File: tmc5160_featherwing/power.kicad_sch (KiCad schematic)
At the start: 0 parts

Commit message: Add connectors
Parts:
- added J1: Conn_TERM_HDR_01x02_Pin_5.0MM_Horizontal, Janelia:PhoenixContact_MSTBA_2,5_2-G_1x02_P5.00mm_Horizontal, symbol Janelia:Conn_TERM_HDR_01x02_Pin_5.0MM_Horizontal
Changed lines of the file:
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@@
   (title_block
     (title "tmc5160_featherwing")
-    (date "2024-03-22")
+    (date "2024-03-25")
     (rev "1.0")
     (company "Howard Hughes Medical Institute")
   )
+  (symbol (lib_id "Janelia:Conn_TERM_HDR_01x02_Pin_5.0MM_Horizontal") (at 73.66 88.9 0) (unit 1)
+    (in_bom yes) (on_board yes) (dnp no) (fields_autoplaced)
+    (property "Reference" "J1" (at 74.295 86.36 0)
+      (effects (font (size 1.27 1.27)))
+    )
+    (property "Value" "Conn_TERM_HDR_01x02_Pin_5.0MM_Horizontal" (at 73.66 101.6 0)
+      (effects (font (size 1.27 1.27)) hide)
+    )
+    (property "Footprint" "Janelia:PhoenixContact_MSTBA_2,5_2-G_1x02_P5.00mm_Horizontal" (at 73.66 53.34 0)
+      (effects (font (size 1.27 1.27)) hide)
+    )
+    (property "Datasheet" "" (at 73.66 67.31 0)
+      (effects (font (size 1.27 1.27)) hide)
+    )
+    (property "Manufacturer" "Phoenix Contact" (at 73.66 55.88 0)
+      (effects (font (size 1.27 1.27)) hide)
+    )
+    (property "Manufacturer Part Number" "1757475" (at 73.66 60.96 0)
+      (effects (font (size 1.27 1.27)) hide)
+    )
+    (property "Description" "TERM BLOCK HDR 2POS 90DEG 5MM" (at 73.66 63.5 0)
+      (effects (font (size 1.27 1.27)) hide)
+    )
+    (property "Vendor" "Digi-Key" (at 73.66 58.42 0)
+      (effects (font (size 1.27 1.27)) hide)
+    )
+    (property "Vendor Part Number" "277-1117-ND" (at 73.66 66.04 0)
+      (effects (font (size 1.27 1.27)) hide)
+    )
+    (property "Sim.Enable" "0" (at 73.66 88.9 0)
+      (effects (font (size 1.27 1.27)) hide)
+    )
+    (pin "1")
+    (pin "2")
+    (instances
+      (project "tmc5160_featherwing"
+        (path "/df2b2e89-e055-4140-95de-f1df723db034/c1dd8f61-494c-402f-8e59-08309c64fc3f"
+          (reference "J1") (unit 1)
+        )
+      )
+    )
+  )
 )

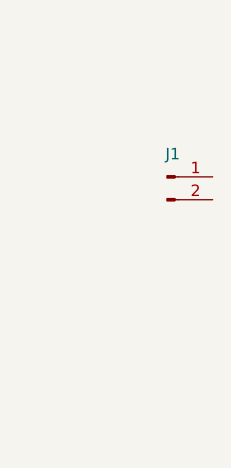
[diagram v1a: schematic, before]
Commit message: Change connectors
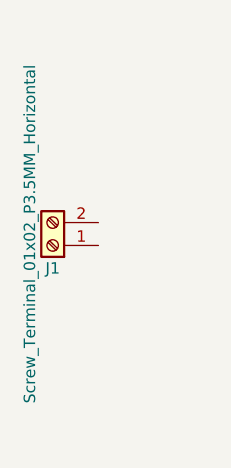
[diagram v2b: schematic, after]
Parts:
- removed J1: Conn_TERM_HDR_01x02_Pin_5.0MM_Horizontal, Janelia:PhoenixContact_MSTBA_2,5_2-G_1x02_P5.00mm_Horizontal, symbol Janelia:Conn_TERM_HDR_01x02_Pin_5.0MM_Horizontal
- added J1: Screw_Terminal_01x02_P3.5MM_Horizontal, Janelia:TerminalBlock_Phoenix_PT-1,5-2-3.5-H_1x02_P3.50mm_Horizontal, symbol Janelia:Screw_Terminal_01x02_P3.5MM_Horizontal
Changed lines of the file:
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@@
     (company "Howard Hughes Medical Institute")
   )
-  (symbol (lib_id "Janelia:Conn_TERM_HDR_01x02_Pin_5.0MM_Horizontal") (at 73.66 88.9 0) (unit 1)
+  (symbol (lib_id "Janelia:Screw_Terminal_01x02_P3.5MM_Horizontal") (at 60.96 96.52 180) (unit 1)
     (in_bom yes) (on_board yes) (dnp no) (fields_autoplaced)
-    (property "Reference" "J1" (at 74.295 86.36 0)
+    (property "Reference" "J1" (at 60.96 99.06 0) (do_not_autoplace)
       (effects (font (size 1.27 1.27)))
     )
-    (property "Value" "Conn_TERM_HDR_01x02_Pin_5.0MM_Horizontal" (at 73.66 101.6 0)
+    (property "Value" "Screw_Terminal_01x02_P3.5MM_Horizontal" (at 58.42 95.25 90) (do_not_autoplace)
+      (effects (font (size 1.27 1.27)))
+    )
+    (property "Footprint" "Janelia:TerminalBlock_Phoenix_PT-1,5-2-3.5-H_1x02_P3.50mm_Horizontal" (at 60.96 96.52 0)
       (effects (font (size 1.27 1.27)) hide)
     )
-    (property "Footprint" "Janelia:PhoenixContact_MSTBA_2,5_2-G_1x02_P5.00mm_Horizontal" (at 73.66 53.34 0)
+    (property "Datasheet" "~" (at 60.96 96.52 0)
       (effects (font (size 1.27 1.27)) hide)
     )
-    (property "Datasheet" "" (at 73.66 67.31 0)
+    (property "Description" "TERM BLK 2POS SIDE ENT 3.5MM PCB" (at 60.96 96.52 0)
       (effects (font (size 1.27 1.27)) hide)
     )
-    (property "Manufacturer" "Phoenix Contact" (at 73.66 55.88 0)
+    (property "Manufacturer" "Phoenix Contact" (at 60.96 96.52 0)
       (effects (font (size 1.27 1.27)) hide)
     )
-    (property "Manufacturer Part Number" "1757475" (at 73.66 60.96 0)
+    (property "Manufacturer Part Number" "1984617" (at 60.96 96.52 0)
       (effects (font (size 1.27 1.27)) hide)
     )
-    (property "Description" "TERM BLOCK HDR 2POS 90DEG 5MM" (at 73.66 63.5 0)
+    (property "Vendor" "Digi-Key" (at 60.96 96.52 0)
       (effects (font (size 1.27 1.27)) hide)
     )
-    (property "Vendor" "Digi-Key" (at 73.66 58.42 0)
+    (property "Vendor Part Number" "277-1721-ND" (at 60.96 96.52 0)
       (effects (font (size 1.27 1.27)) hide)
     )
-    (property "Vendor Part Number" "277-1117-ND" (at 73.66 66.04 0)
-      (effects (font (size 1.27 1.27)) hide)
-    )
-    (property "Sim.Enable" "0" (at 73.66 88.9 0)
-      (effects (font (size 1.27 1.27)) hide)
-    )

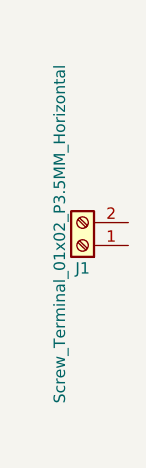
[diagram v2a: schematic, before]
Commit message: Switch back to terminal blocks
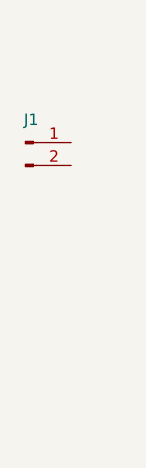
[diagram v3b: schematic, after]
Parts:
- removed J1: Screw_Terminal_01x02_P3.5MM_Horizontal, Janelia:TerminalBlock_Phoenix_PT-1,5-2-3.5-H_1x02_P3.50mm_Horizontal, symbol Janelia:Screw_Terminal_01x02_P3.5MM_Horizontal
- added J1: Conn_TERM_HDR_01x02_Pin_3.5MM_Horizontal, Janelia:PhoenixContact_MC_1,5_2-G-3.5_1x02_P3.50mm_Horizontal, symbol Janelia:Conn_TERM_HDR_01x02_Pin_3.5MM_Horizontal
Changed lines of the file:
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@@
     (company "Howard Hughes Medical Institute")
   )
-  (symbol (lib_id "Janelia:Screw_Terminal_01x02_P3.5MM_Horizontal") (at 60.96 96.52 180) (unit 1)
+  (symbol (lib_id "Janelia:Conn_TERM_HDR_01x02_Pin_3.5MM_Horizontal") (at 54.61 85.09 0) (unit 1)
     (in_bom yes) (on_board yes) (dnp no) (fields_autoplaced)
-    (property "Reference" "J1" (at 60.96 99.06 0) (do_not_autoplace)
+    (property "Reference" "J1" (at 55.245 82.55 0)
       (effects (font (size 1.27 1.27)))
     )
-    (property "Value" "Screw_Terminal_01x02_P3.5MM_Horizontal" (at 58.42 95.25 90) (do_not_autoplace)
-      (effects (font (size 1.27 1.27)))
-    )
-    (property "Footprint" "Janelia:TerminalBlock_Phoenix_PT-1,5-2-3.5-H_1x02_P3.50mm_Horizontal" (at 60.96 96.52 0)
+    (property "Value" "Conn_TERM_HDR_01x02_Pin_3.5MM_Horizontal" (at 54.61 97.79 0)
       (effects (font (size 1.27 1.27)) hide)
     )
-    (property "Datasheet" "~" (at 60.96 96.52 0)
+    (property "Footprint" "Janelia:PhoenixContact_MC_1,5_2-G-3.5_1x02_P3.50mm_Horizontal" (at 54.61 49.53 0)
       (effects (font (size 1.27 1.27)) hide)
     )
-    (property "Description" "TERM BLK 2POS SIDE ENT 3.5MM PCB" (at 60.96 96.52 0)
+    (property "Datasheet" "" (at 54.61 63.5 0)
       (effects (font (size 1.27 1.27)) hide)
     )
-    (property "Manufacturer" "Phoenix Contact" (at 60.96 96.52 0)
+    (property "Manufacturer" "Phoenix Contact" (at 54.61 52.07 0)
       (effects (font (size 1.27 1.27)) hide)
     )
-    (property "Manufacturer Part Number" "1984617" (at 60.96 96.52 0)
+    (property "Manufacturer Part Number" "1844210" (at 54.61 57.15 0)
       (effects (font (size 1.27 1.27)) hide)
     )
-    (property "Vendor" "Digi-Key" (at 60.96 96.52 0)
+    (property "Description" "TERM BLOCK HDR 2POS 90DEG 3.5MM" (at 54.61 59.69 0)
       (effects (font (size 1.27 1.27)) hide)
     )
-    (property "Vendor Part Number" "277-1721-ND" (at 60.96 96.52 0)
+    (property "Vendor" "Digi-Key" (at 54.61 54.61 0)
       (effects (font (size 1.27 1.27)) hide)
     )
+    (property "Vendor Part Number" "277-2416-ND" (at 54.61 62.23 0)
+      (effects (font (size 1.27 1.27)) hide)
+    )
+    (property "Sim.Enable" "0" (at 54.61 85.09 0)
+      (effects (font (size 1.27 1.27)) hide)
+    )
+    (pin "2")
     (pin "1")
-    (pin "2")
     (instances
       (project "tmc5160_featherwing"

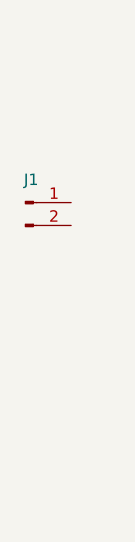
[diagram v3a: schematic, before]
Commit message: Adjust connectors
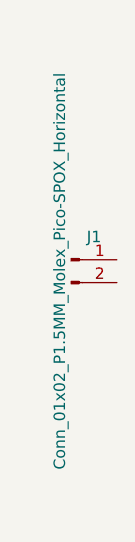
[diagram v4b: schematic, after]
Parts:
- removed J1: Conn_TERM_HDR_01x02_Pin_3.5MM_Horizontal, Janelia:PhoenixContact_MC_1,5_2-G-3.5_1x02_P3.50mm_Horizontal, symbol Janelia:Conn_TERM_HDR_01x02_Pin_3.5MM_Horizontal
- added J1: Conn_01x02_P1.5MM_Molex_Pico-SPOX_Horizontal, Janelia:Molex_Pico-SPOX_87438_1x02-P1.5MM_Horizontal, symbol Janelia:Conn_01x02_P1.5MM_Molex_Pico-SPOX_Horizontal
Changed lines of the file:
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@@
   (title_block
     (title "tmc5160_featherwing")
-    (date "2024-03-25")
+    (date "2024-04-04")
     (rev "1.0")
     (company "Howard Hughes Medical Institute")
   )
-  (symbol (lib_id "Janelia:Conn_TERM_HDR_01x02_Pin_3.5MM_Horizontal") (at 54.61 85.09 0) (unit 1)
+  (symbol (lib_id "Janelia:Conn_01x02_P1.5MM_Molex_Pico-SPOX_Horizontal") (at 59.69 91.44 0) (unit 1)
     (in_bom yes) (on_board yes) (dnp no) (fields_autoplaced)
-    (property "Reference" "J1" (at 55.245 82.55 0)
+    (property "Reference" "J1" (at 62.23 88.9 0) (do_not_autoplace)
       (effects (font (size 1.27 1.27)))
     )
-    (property "Value" "Conn_TERM_HDR_01x02_Pin_3.5MM_Horizontal" (at 54.61 97.79 0)
+    (property "Value" "Conn_01x02_P1.5MM_Molex_Pico-SPOX_Horizontal" (at 58.42 92.71 90) (do_not_autoplace)
+      (effects (font (size 1.27 1.27)))
+    )
+    (property "Footprint" "Janelia:Molex_Pico-SPOX_87438_1x02-P1.5MM_Horizontal" (at 59.69 91.44 0)
       (effects (font (size 1.27 1.27)) hide)
     )
-    (property "Footprint" "Janelia:PhoenixContact_MC_1,5_2-G-3.5_1x02_P3.50mm_Horizontal" (at 54.61 49.53 0)
+    (property "Datasheet" "~" (at 59.69 91.44 0)
       (effects (font (size 1.27 1.27)) hide)
     )
-    (property "Datasheet" "" (at 54.61 63.5 0)
+    (property "Description" "CONN HEADER SMD R/A 2POS 1.5MM" (at 59.69 91.44 0)
       (effects (font (size 1.27 1.27)) hide)
     )
-    (property "Manufacturer" "Phoenix Contact" (at 54.61 52.07 0)
+    (property "Manufacturer" "Molex" (at 59.69 91.44 0)
       (effects (font (size 1.27 1.27)) hide)
     )
-    (property "Manufacturer Part Number" "1844210" (at 54.61 57.15 0)
+    (property "Manufactuer Part Number" "0874380243" (at 59.69 91.44 0)
       (effects (font (size 1.27 1.27)) hide)
     )
-    (property "Description" "TERM BLOCK HDR 2POS 90DEG 3.5MM" (at 54.61 59.69 0)
+    (property "Vendor" "Digi-Key" (at 59.69 91.44 0)
       (effects (font (size 1.27 1.27)) hide)
     )
-    (property "Vendor" "Digi-Key" (at 54.61 54.61 0)
+    (property "Vendor Part Number" "WM7646CT-ND" (at 59.69 91.44 0)
       (effects (font (size 1.27 1.27)) hide)
     )
-    (property "Vendor Part Number" "277-2416-ND" (at 54.61 62.23 0)
-      (effects (font (size 1.27 1.27)) hide)
-    )
-    (property "Sim.Enable" "0" (at 54.61 85.09 0)
-      (effects (font (size 1.27 1.27)) hide)
-    )
+    (pin "1")
     (pin "2")
-    (pin "1")
     (instances
       (project "tmc5160_featherwing"

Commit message: Add to power sheet
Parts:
- removed J1: Conn_01x02_P1.5MM_Molex_Pico-SPOX_Horizontal, Janelia:Molex_Pico-SPOX_87438_1x02-P1.5MM_Horizontal, symbol Janelia:Conn_01x02_P1.5MM_Molex_Pico-SPOX_Horizontal
- added C1: 100uF_63V, Janelia:CP_Elec_10x10.5, symbol Janelia:CP_100uF_63V_10x10.5MM
- added C2: 10uF_100V, Janelia:C_1210_3225Metric, symbol Janelia:C_10uF_100V_1210
- added C3: 10uF_6.3V, Janelia:C_0402_1005Metric, symbol Janelia:C_10uF_6.3V_0402
- added J1, J3: Conn_01x03_P2.54MM_HeaderHoles, Janelia:PinHeader_1x03_P2.54mm_Vertical_Holes, symbol Janelia:Conn_01x03_P2.54MM_HeaderHoles
- added J2: Conn_01x02_P1.5MM_Molex_Pico-SPOX-87438_Horizontal, Janelia:Molex_Pico-SPOX-87438_1x02-P1.5MM_Horizontal, symbol Janelia:Conn_01x02_P1.5MM_Molex_Pico-SPOX-87438_Horizontal
- added U10: 3.3V_100MA, Janelia:DRB0008B, symbol Janelia:Regulator_Linear_3.3V_100MA_60Vin
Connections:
- new net ENABLE: U10.5 (EN)
- new net GND: C1.2, C2.2, C3.2, J2.2 (Pin_2), J3.1 (Pin_1), J3.2 (Pin_2), J3.3 (Pin_3), U10.4 (GND), U10.9 (PAD)
- new net VIO: C3.1, U10.1 (OUT)
- new net VM: C1.1, C2.1, J1.1 (Pin_1), J1.2 (Pin_2), J1.3 (Pin_3), J2.1 (Pin_1), U10.8 (IN)
- no-connect marks 0 -> 2

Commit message: Add parts
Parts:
- added C2: 100uF_63V, Janelia:CP_Elec_10x10.5, symbol Janelia:CP_100uF_63V_10x10.5MM
- added D1: Diode_SMAJ51A, Janelia:D_SMA, symbol Janelia:Diode_SMAJ51A
- renumbered C2 to C3, C3 to C4
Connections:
- net GND: now also J1.1 (Pin_1), J1.2 (Pin_2), J1.3 (Pin_3), J2.1 (Pin_1), C2.2, D1.2 (A2); no longer J2.2 (Pin_2), J3.1 (Pin_1), J3.2 (Pin_2), J3.3 (Pin_3)
- net VM: now also J2.2 (Pin_2), J3.1 (Pin_1), J3.2 (Pin_2), J3.3 (Pin_3), C2.1, D1.1 (A1); no longer J1.1 (Pin_1), J1.2 (Pin_2), J1.3 (Pin_3), J2.1 (Pin_1)
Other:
- moved on the sheet: C3, C4, J1, J2, J3, U10

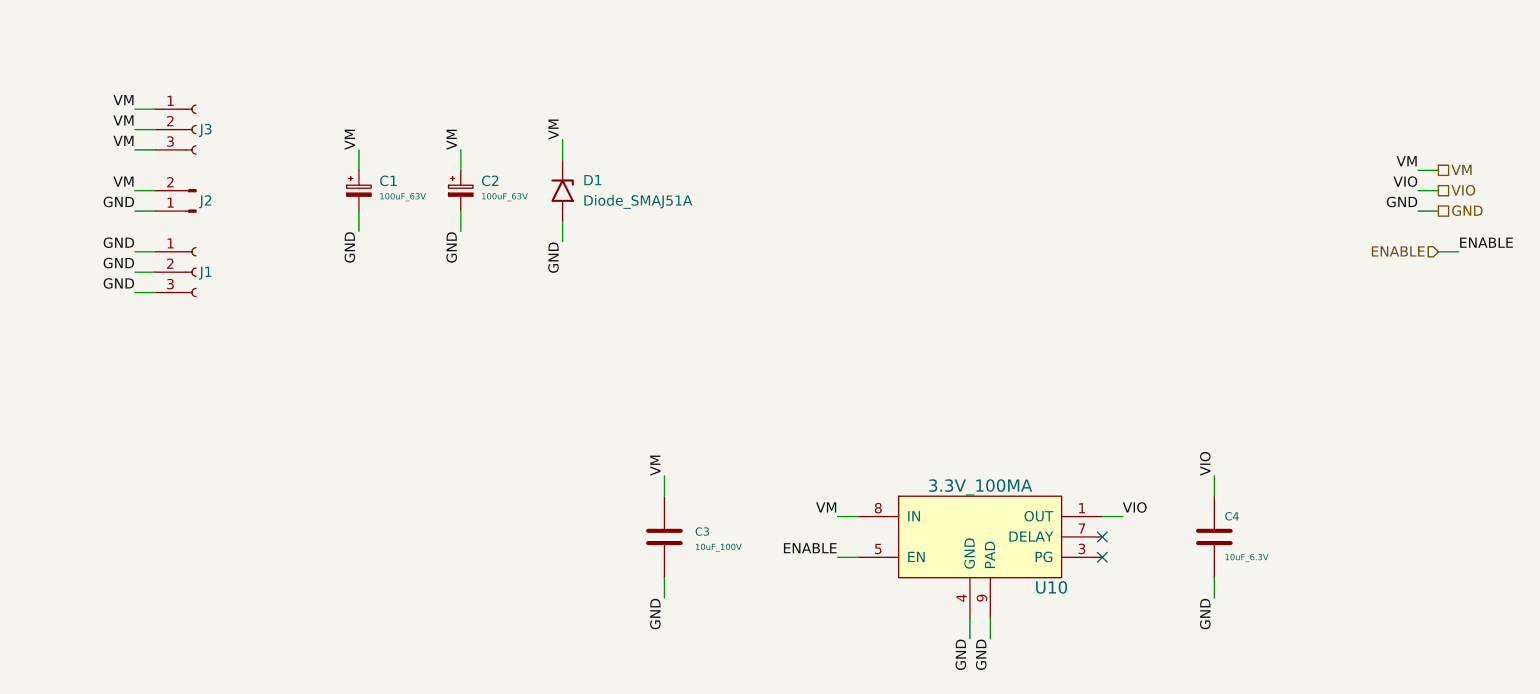
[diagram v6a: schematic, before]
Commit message: Add capactitors
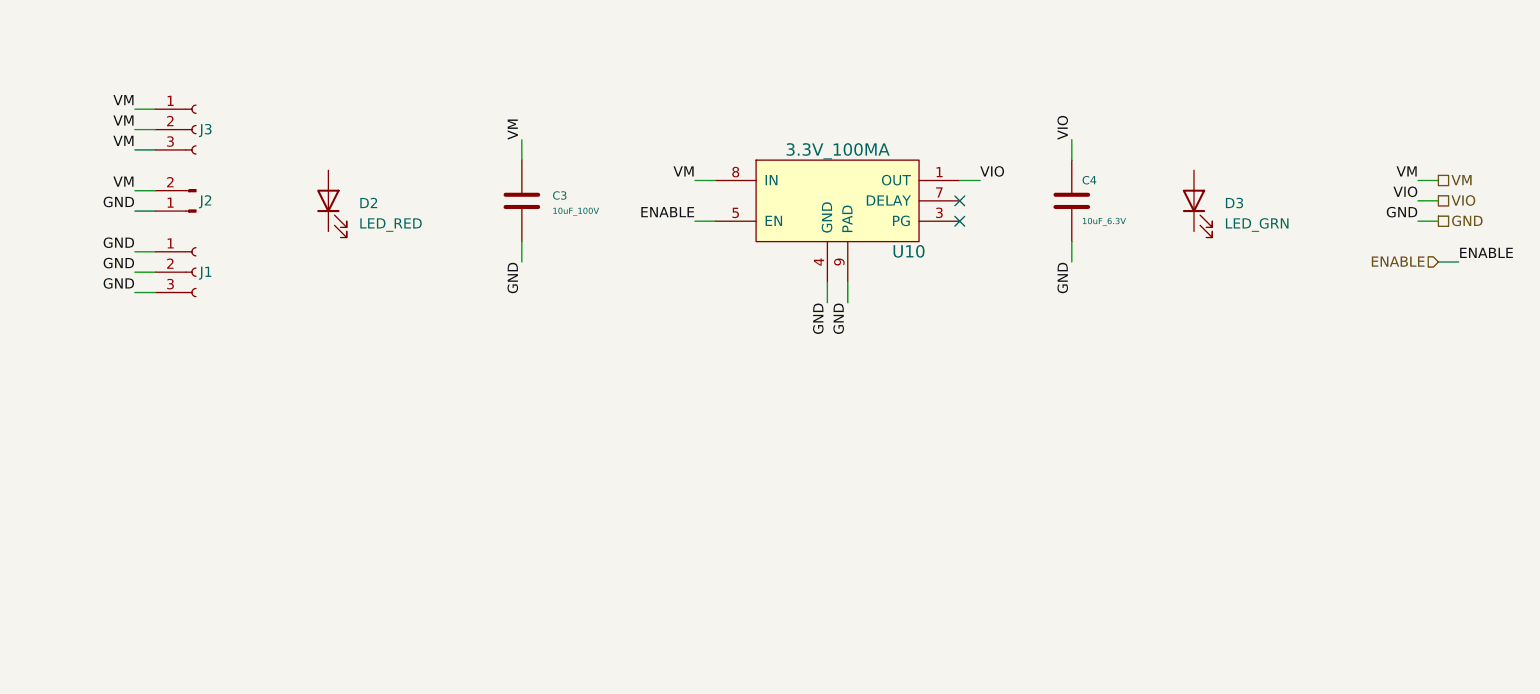
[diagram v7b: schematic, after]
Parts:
- removed C1, C2: 100uF_63V, Janelia:CP_Elec_10x10.5, symbol Janelia:CP_100uF_63V_10x10.5MM
- removed D1: Diode_SMAJ51A, Janelia:D_SMA, symbol Janelia:Diode_SMAJ51A
- added D2: LED_RED, Janelia:LED_0402_1005Metric, symbol Janelia:LED_QT_RED_2V_0402
- added D3: LED_GRN, Janelia:LED_0402_1005Metric, symbol Janelia:LED_QT_GRN_2V_0402
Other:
- moved on the sheet: C3, C4, U10

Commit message: Add capacitors and resistors
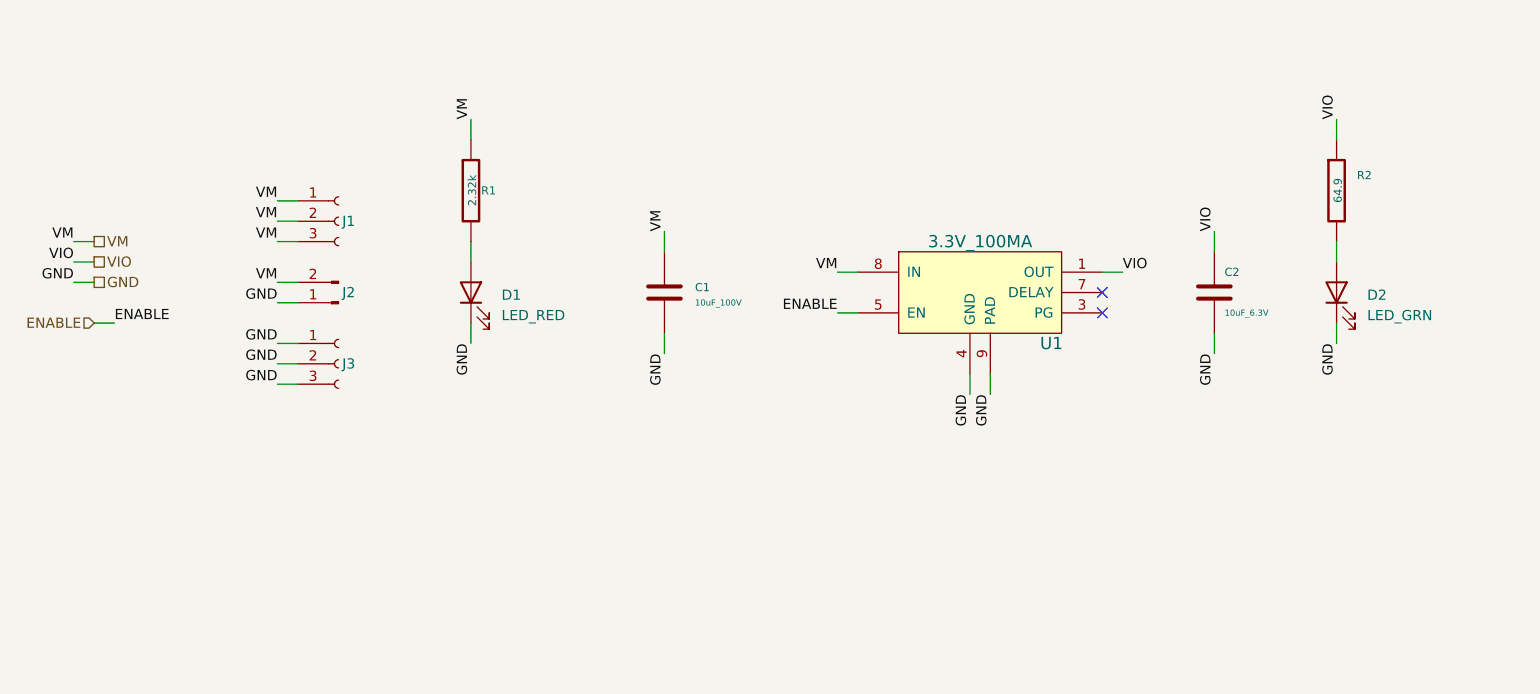
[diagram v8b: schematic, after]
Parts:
- added R1: 2.32k, R_0805_2012Metric.kicad_mod, symbol Janelia:R_2.32k_1W_0805
- added R2: 64.9, Janelia:R_0402_1005Metric, symbol Janelia:R_64.9_0.1W_0402
- renumbered C3 to C1, C4 to C2, D2 to D1, D3 to D2, J3 to J1, J1 to J3, U10 to U1
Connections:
- net GND: now also D1.1 (K), D2.1 (K)
- net VIO: now also R2.1
- net VM: now also R1.1
- net at D2.2 (A): now also R2.2
- net at D1.2 (A): now also R1.2
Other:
- moved on the sheet: C1, C2, D1, D2, J1, J2, J3, U1
